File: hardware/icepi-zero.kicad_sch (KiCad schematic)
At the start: 7 parts, among them J1 Micro_SD_Card_Det2, J2 Conn_02x20_Counter_Clockwise, U1 ECP5U_12_CABGA256

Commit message: Routed most of sdram
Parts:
- removed unit 5 of U1
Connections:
- net A10: now reaches U1.A10 (PT42B/-)
- net BA0: now reaches U1.A11 (PT53A/+)
- net ~{RAS}: now reaches U1.A12 (PT53B/-)
- net ~{WE}: now reaches U1.A13 (PT65A/+)
- net D7: now reaches U1.A14 (PT65B/-)
- net D5: now reaches U1.A15 (PT67B/-)
- net A1: now reaches U1.A9 (PT42A/+)
- net A0: now reaches U1.B10 (PT44A/+)
- net BA1: now reaches U1.B11 (PT49A/+)
- net ~{CS}: now reaches U1.B12 (PT56A/+)
- net ~{CAS}: now reaches U1.B13 (PT60A/+)
- net DQM0: now reaches U1.B14 (PT67A/+)
- net A4: now reaches U1.B8 (PT35B/-/PCLKC1_0)
- net A2: now reaches U1.B9 (PT38A/+/GR_PCLK1_0)
- net GLOBAL_CLK: now reaches U1.M2 (PL26D/-/PCLKC6_0/LDQ32)
- net D6: now reaches U1.B15 (PR2B/-/S0_IN/HS/RDQ8)
- net D0: now reaches U1.B16 (PR2A/+/HS/RDQ8)
- net D1: now reaches U1.C14 (PR2C/+/RDQ8)
- net D3: now reaches U1.C15 (PR5B/-/HS/RDQ8)
- net D2: now reaches U1.C16 (PR5A/+/HS/RDQ8)
- net D4: now reaches U1.D16 (PR8A/+/HS/RDQS8)
- net D8: now reaches U1.A2 (PT4A/+)
- net CLK: now reaches U1.A3 (PT6A/+)
- net A12: now reaches U1.A4 (PT6B/-)
- net A9: now reaches U1.A5 (PT18A/+)
- net A7: now reaches U1.A6 (PT18B/-)
- net A5: now reaches U1.A7 (PT29A/+/PCLKT0_0)
- net A3: now reaches U1.A8 (PT29B/-/PCLKC0_0)
- net DQM1: now reaches U1.B3 (PT4B/-)
- net CKE: now reaches U1.B4 (PT11B/-)
- net A11: now reaches U1.B5 (PT15B/-)
- net A8: now reaches U1.B6 (PT22B/-)
- net A6: now reaches U1.B7 (PT27B/-/PCLKC0_1)
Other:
- note added: "Maybe add a wifi module"

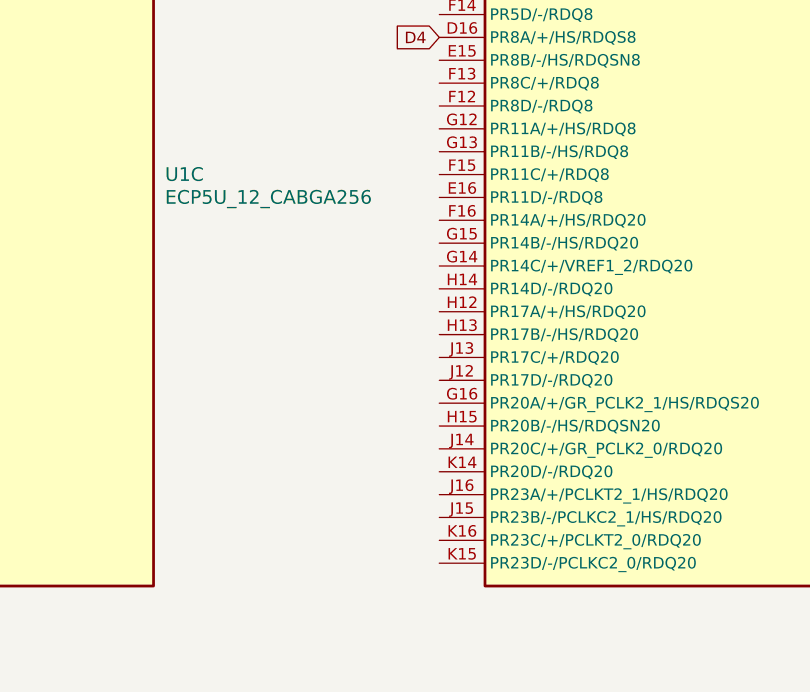
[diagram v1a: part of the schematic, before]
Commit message: Routed power
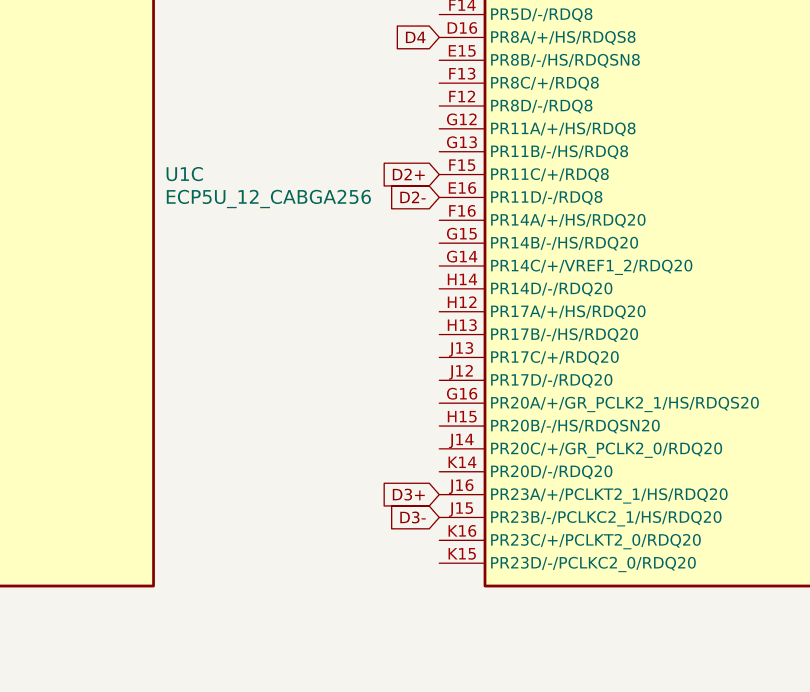
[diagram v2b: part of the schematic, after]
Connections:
- net D2-: now reaches U1.E16 (PR11D/-/RDQ8)
- net D2+: now reaches U1.F15 (PR11C/+/RDQ8)
- net D3-: now reaches U1.J15 (PR23B/-/PCLKC2_1/HS/RDQ20)
- net D3+: now reaches U1.J16 (PR23A/+/PCLKT2_1/HS/RDQ20)
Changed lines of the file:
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@@
+		)
+	)
+	(global_label "D2+"
+		(shape input)
+		(at 416.56 52.07 180)
+		(fields_autoplaced yes)
+		(effects
+			(font
+				(size 1.27 1.27)
+			)
+			(justify right)
+		)
+		(property "Intersheetrefs" "${INTERSHEET_REFS}"
+			(at 409.5229 52.07 0)
+			(effects
+				(font
+					(size 1.27 1.27)
+				)
+				(justify right)
+				(hide yes)
+			)
 		)
 	)
@@
 		)
 	)
+	(global_label "D3-"
+		(shape input)
+		(at 416.56 90.17 180)
+		(fields_autoplaced yes)
+		(effects
+			(font
+				(size 1.27 1.27)
+			)
+			(justify right)
+		)
+		(property "Intersheetrefs" "${INTERSHEET_REFS}"
+			(at 409.5229 90.17 0)
+			(effects
+				(font
+					(size 1.27 1.27)
+				)
+				(justify right)
+				(hide yes)
+			)
+		)
+	)
 	(global_label "A6"
 		(shape input)
@@
 			(effects
 				(font
+					(size 1.27 1.27)
+				)
+				(justify right)
+				(hide yes)
+			)
+		)
+	)
+	(global_label "D2-"
+		(shape input)
+		(at 416.56 54.61 180)
+		(fields_autoplaced yes)
+		(effects
+			(font
+				(size 1.27 1.27)
+			)
+			(justify right)
+		)
+		(property "Intersheetrefs" "${INTERSHEET_REFS}"
+			(at 409.5229 54.61 0)
+			(effects
+				(font
+					(size 1.27 1.27)
+				)
+				(justify right)
+				(hide yes)
+			)
+		)
+	)
+	(global_label "D3+"
+		(shape input)
+		(at 416.56 87.63 180)
+		(fields_autoplaced yes)
+		(effects
+			(font
+				(size 1.27 1.27)
+			)
+			(justify right)
+		)
+		(property "Intersheetrefs" "${INTERSHEET_REFS}"
+			(at 409.5229 87.63 0)
+			(effects
+				(font

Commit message: Added the decoupling capacitors
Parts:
- added C35, C41, C42: 10uF, Capacitor_SMD:C_0603_1608Metric, symbol Device:C_Small
- added C36, C37, C39, C40: 100nF, Capacitor_SMD:C_0402_1005Metric, symbol Device:C_Small
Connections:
- net +3V3: now also J1.4 (VDD), U1.F10 (VCCIO1[2]), U1.F11 (VCCIO1[2]), U1.F6 (VCCIO0[2]), U1.F7 (VCCIO0[2]), U1.H11 (VCCIO2[2]), U1.J11 (VCCIO2[2]), U1.J6 (VCCIO6[2]), U1.J7 (VCCIO6[2]), C35.1, C36.1, C37.1, C39.1, C40.1, C41.1, C42.1
- net CLK: now also J1.5 (CLK)
- net GND: now also J1.11 (SHIELD), J1.6 (VSS), J1.9 (DET_B), C35.2, C36.2, C37.2, C39.2, C40.2, C41.2, C42.2
- net GPIO_10: now reaches J2.10 (Pin_10)
- net GPIO_10: now also U1.N1 (PL32A/+/HS/LDQS32)
- net GPIO_11: now reaches J2.11 (Pin_11)
- net GPIO_11: now also U1.R4 (PL41C/+/LDQ44)
- net GPIO_12: now reaches J2.12 (Pin_12)
- net GPIO_12: now also U1.N4 (PL38A/+/HS/LDQ44)
- net GPIO_13: now reaches J2.13 (Pin_13)
- net GPIO_13: now also U1.P4 (PL41A/+/HS/LDQ44)
- net GPIO_15: now reaches J2.15 (Pin_15)
- net GPIO_15: now also U1.P2 (PL32B/-/HS/LDQSN32)
- net GPIO_16: now reaches J2.16 (Pin_16)
- net GPIO_16: now also U1.M1 (PL26C/+/PCLKT6_0/LDQ32)
- net GPIO_18: now reaches J2.18 (Pin_18)
- net GPIO_18: now also U1.L1 (PL26A/+/PCLKT6_1/HS/LDQ32)
- net GPIO_19: now reaches J2.19 (Pin_19)
- net GPIO_21: now reaches J2.21 (Pin_21)
- net GPIO_22: now reaches J2.22 (Pin_22)
- net GPIO_23: now reaches J2.23 (Pin_23)
- net GPIO_24: now reaches J2.24 (Pin_24)
- net GPIO_26: now reaches J2.26 (Pin_26)
- net GPIO_27: now reaches J2.27 (Pin_27)
- net GPIO_28: now reaches J2.28 (Pin_28)
- net GPIO_29: now reaches J2.29 (Pin_29)
- net GPIO_3: now reaches J2.3 (Pin_3)
- net GPIO_3: now also U1.T2 (PL38D/-/LDQ44)
- net GPIO_31: now reaches J2.31 (Pin_31)
- net GPIO_32: now reaches J2.32 (Pin_32)
- net GPIO_33: now reaches J2.33 (Pin_33)
- net GPIO_35: now reaches J2.35 (Pin_35)
- net GPIO_36: now reaches J2.36 (Pin_36)
- net GPIO_37: now reaches J2.37 (Pin_37)
- net GPIO_37: now also U1.C4 (PT11A/+)
- net GPIO_38: now reaches J2.38 (Pin_38)
- net GPIO_40: now reaches J2.40 (Pin_40)
- net GPIO_5: now reaches J2.5 (Pin_5)
- net GPIO_5: now also U1.R2 (PL38C/+/LDQ44)
- net GPIO_7: now reaches J2.7 (Pin_7)
- net GPIO_7: now also U1.R1 (PL35B/-/VREF1_6/HS/LDQ32)
- net GPIO_8: now reaches J2.8 (Pin_8)
- net GPIO_8: now also U1.P1 (PL35A/+/HS/LDQ32)
- net FPDI_SCL: now reaches U1.T3 (PL41D/-/LDQ44)
- net FPDI_SDA: now reaches U1.T4 (PL44B/-/HS/LDQSN44)
- net DAT2: now reaches J1.1 (DAT2)
- net DET: now reaches J1.10 (DET_A)
- net DAT3: now reaches J1.2 (DAT3/CD)
- net CMD: now reaches J1.3 (CMD)
- net DAT0: now reaches J1.7 (DAT0)
- net DAT1: now reaches J1.8 (DAT1)
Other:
- moved on the sheet: J1

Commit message: V1.0 Final Revision and Readme documentation
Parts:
- removed C37, C39, C40: 100nF, Capacitor_SMD:C_0402_1005Metric, symbol Device:C_Small
- removed C41, C42: 10uF, Capacitor_SMD:C_0603_1608Metric, symbol Device:C_Small
- removed J1: Micro_SD_Card_Det2, icepi-lib:microSD_HC_SOFNG_TF-008, symbol Connector:Micro_SD_Card_Det2
- removed U1: ECP5U_12_CABGA256, Package_BGA:BGA-256_14.0x14.0mm_Layout16x16_P0.8mm_Ball0.45mm_Pad0.32mm_NSMD, symbol josh:ECP5U_12_CABGA256
- added D1, D2, D3, D4: WHITE, LED_SMD:LED_0603_1608Metric, symbol Device:LED
- added R1, R2, R3, R4: 470, Resistor_SMD:R_0402_1005Metric, symbol Device:R
- added TP1, TP2, TP3, TP4, TP5, TP6: TestPoint, TestPoint:TestPoint_Pad_D2.0mm, symbol Connector:TestPoint
- added U3: ECP5U_12_CABGA256, Package_BGA:BGA-256_14.0x14.0mm_Layout16x16_P0.8mm_Ball0.45mm_Pad0.32mm_NSMD, symbol josh:ECP5U_12_CABGA256
- renumbered C35 to C47, C36 to C48, J2 to J1
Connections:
- net +3V3: now also TP2.1, U3.J6 (VCCIO6[2]), U3.J7 (VCCIO6[2])
- net +5V: now also TP1.1
- net FPDI_SCL: now also U3.T3 (PL41D/-/LDQ44)
- net FPDI_SDA: now also U3.T4 (PL44B/-/HS/LDQSN44)
- net GLOBAL_CLK: now also U3.M2 (PL26D/-/PCLKC6_0/LDQ32)
- net GND: now also D1.1 (K), D2.1 (K), D3.1 (K), D4.1 (K), TP4.1, TP5.1
- net GPIO_10: now also U3.N1 (PL32A/+/HS/LDQS32)
- net GPIO_11: now also U3.R3 (PL41B/-/HS/LDQ44)
- net GPIO_12: now also U3.N4 (PL38A/+/HS/LDQ44)
- net GPIO_13: now also U3.P3 (PL38B/-/HS/LDQ44)
- net GPIO_15: now also U3.P2 (PL32B/-/HS/LDQSN32)
- net GPIO_16: now also U3.M1 (PL26C/+/PCLKT6_0/LDQ32)
- net GPIO_18: now also U3.L1 (PL26A/+/PCLKT6_1/HS/LDQ32)
- net GPIO_3: now also U3.T2 (PL38D/-/LDQ44)
- net GPIO_5: now also U3.R2 (PL38C/+/LDQ44)
- net GPIO_7: now also U3.R1 (PL35B/-/VREF1_6/HS/LDQ32)
- net GPIO_8: now also U3.P1 (PL35A/+/HS/LDQ32)
- new net: D1.2 (A), R1.2
- new net: D2.2 (A), R2.2
- new net: D4.2 (A), R4.2
- new net: D3.2 (A), R3.2
- new net +1V1: TP3.1
- new net +2V5: TP6.1
- new net FPDI_CEC: U3.R5 (PL44A/+/HS/LDQS44)
- new net FPDI_UTIL: U3.P5 (PL47D/-/LLC_GPLL0C_IN/LDQ44)
- new net LED1: R1.1
- new net LED2: R2.1
- new net LED3: R3.1
- new net LED4: R4.1
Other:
- added sheet ECP5 (ecp5.kicad_sch)
- note removed: "TODO: Check out how to add WiFI"
- moved on the sheet: C47, C48, H1, H2, H3, H4

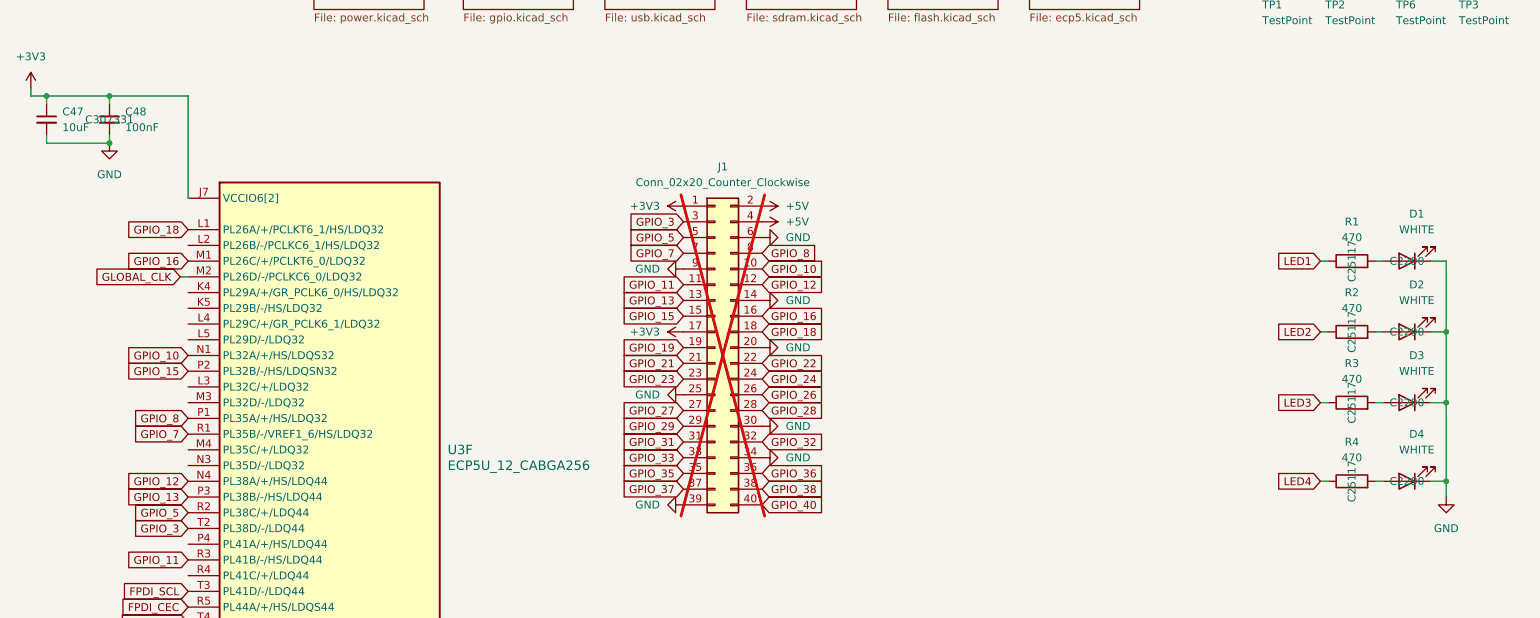
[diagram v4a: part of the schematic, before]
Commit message: Fix level shifter EN voltage error
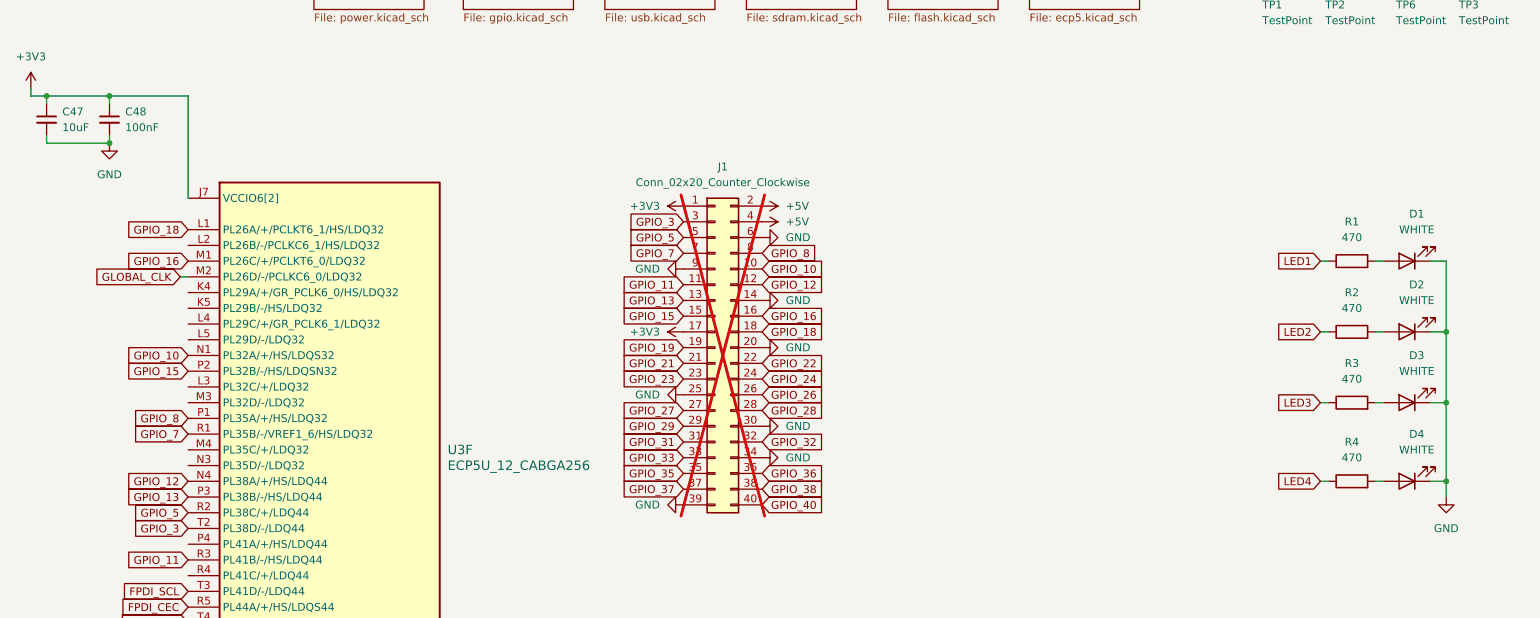
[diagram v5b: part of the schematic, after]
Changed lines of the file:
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@@
 					(size 1.27 1.27)
 				)
+				(hide yes)
 			)
 		)
@@
 					(size 1.27 1.27)
 				)
+				(hide yes)
 			)
 		)
@@
 					(size 1.27 1.27)
 				)
+				(hide yes)
 			)
 		)
@@
 					(size 1.27 1.27)
 				)
+				(hide yes)
 			)
 		)
@@
 					(size 1.27 1.27)
 				)
+				(hide yes)
 			)
 		)
@@
 					(size 1.27 1.27)
 				)
+				(hide yes)
 			)
 		)
@@
 					(size 1.27 1.27)
 				)
+				(hide yes)
 			)
 		)
@@
 					(size 1.27 1.27)
 				)
+				(hide yes)
 			)
 		)
@@
 					(size 1.27 1.27)
 				)
-			)
-		)
+				(hide yes)
+			)
+		)

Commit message: Add a revision
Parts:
- TP1, TP2, TP3, TP4, TP5, TP6: now not fitted
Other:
- note removed: "Maybe add a wifi module"
- moved on the sheet: D1, D2, D3, D4, R1, R2, R3, R4

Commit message: Pre-prod fixes
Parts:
- added D6: WHITE, LED_SMD:LED_0603_1608Metric, symbol Device:LED
- added R34: 470, Resistor_SMD:R_0402_1005Metric, symbol Device:R
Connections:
- net GND: now also D6.1 (K)
- net GPIO_19: now also U3.L2 (PL26B/-/PCLKC6_1/HS/LDQ32)
- net LED2: now also R4.1; no longer R2.1
- net LED3: now also R2.1; no longer R3.1
- net LED4: now also R3.1; no longer R4.1
- new net: D6.2 (A), R34.2
- new net LED5: R34.1

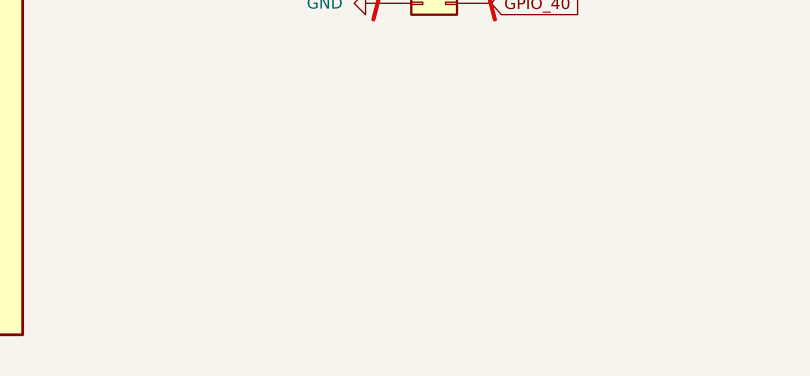
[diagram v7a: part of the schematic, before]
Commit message: Add a button
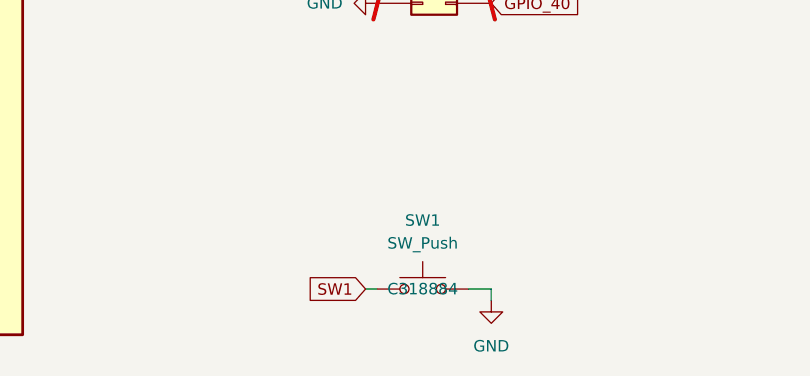
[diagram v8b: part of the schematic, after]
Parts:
- added SW1: SW_Push, Button_Switch_SMD:SW_SPST_TL3342, symbol Switch:SW_Push
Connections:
- net GND: now also SW1.2
- new net SW1: SW1.1
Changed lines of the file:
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@@
 	(wire
 		(pts
+			(xy 139.7 176.53) (xy 142.24 176.53)
+		)
+		(stroke
+			(width 0)
+			(type default)
+		)
+	)
+	(wire
+		(pts
 			(xy 203.2 113.03) (xy 204.47 113.03)
 		)
@@
 	(wire
 		(pts
+			(xy 142.24 177.8) (xy 142.24 176.53)
+		)
+		(stroke
+			(width 0)
+			(type default)
+		)
+	)
+	(wire
+		(pts
 			(xy 212.09 113.03) (xy 213.36 113.03)
 		)
@@
 	(wire
 		(pts
+			(xy 128.27 176.53) (xy 129.54 176.53)
+		)
+		(stroke
+			(width 0)
+			(type default)
+		)
+	)
+	(wire
+		(pts
 			(xy 212.09 137.16) (xy 213.36 137.16)
 		)
@@
 		)
 	)
+	(global_label "SW1"
+		(shape input)
+		(at 128.27 176.53 180)
+		(fields_autoplaced yes)
+		(effects
+			(font
+				(size 1.27 1.27)
+			)
+			(justify right)
+		)
+		(property "Intersheetrefs" "${INTERSHEET_REFS}"
+			(at 121.4144 176.53 0)
+			(effects
+				(font
+					(size 1.27 1.27)
+				)
+				(justify right)
+				(hide yes)
+			)
+		)
+	)
 	(global_label "LED1"
 		(shape input)
@@
 	)
 	(symbol
+		(lib_id "power:GND")
+		(at 142.24 177.8 0)
+		(unit 1)
+		(exclude_from_sim no)
+		(in_bom yes)
+		(on_board yes)
+		(dnp no)
+		(fields_autoplaced yes)
+		(property "Reference" "#PWR0100"
+			(at 142.24 184.15 0)
+			(effects
+				(font
+					(size 1.27 1.27)
+				)
+				(hide yes)
+			)
+		)
+		(property "Value" "GND"
+			(at 142.24 182.88 0)
+			(effects
+				(font
+					(size 1.27 1.27)
+				)
+			)
+		)
+		(property "Footprint" ""
+			(at 142.24 177.8 0)
+			(effects
+				(font
+					(size 1.27 1.27)
+				)
+				(hide yes)
+			)
+		)
+		(property "Datasheet" ""
+			(at 142.24 177.8 0)
+			(effects
+				(font
+					(size 1.27 1.27)
+				)
+				(hide yes)
+			)
+		)
+		(property "Description" "Power symbol creates a global label with name \"GND\" , ground"
+			(at 142.24 177.8 0)
+			(effects
+				(font
+					(size 1.27 1.27)
+				)
+				(hide yes)
+			)
+		)
+		(pin "1"
+		)
+		(instances
+			(project ""
+				(path "/f88da08e-cf42-4d03-a08f-3f602fe6658d"
+					(reference "#PWR0100")
+					(unit 1)
+				)
+			)
+		)
+	)
+	(symbol
 		(lib_id "josh:ECP5U_12_CABGA256")
 		(at 71.12 133.35 0)
@@
 					(unit 1)
 				)
+			)
+		)
+	)
+	(symbol
+		(lib_id "Switch:SW_Push")
+		(at 134.62 176.53 0)
+		(unit 1)
+		(exclude_from_sim no)
+		(in_bom yes)
+		(on_board yes)
+		(dnp no)
+		(fields_autoplaced yes)
+		(property "Reference" "SW1"
+			(at 134.62 168.91 0)
+			(effects
+				(font
+					(size 1.27 1.27)
+				)
+			)
+		)
+		(property "Value" "SW_Push"
+			(at 134.62 171.45 0)
+			(effects
+				(font
+					(size 1.27 1.27)
+				)
+			)
+		)
+		(property "Footprint" "Button_Switch_SMD:SW_SPST_TL3342"
+			(at 134.62 171.45 0)
+			(effects
+				(font
+					(size 1.27 1.27)
+				)
+				(hide yes)
+			)
+		)
+		(property "Datasheet" "~"
+			(at 134.62 171.45 0)
+			(effects
+				(font
+					(size 1.27 1.27)
+				)
+				(hide yes)
+			)
+		)
+		(property "Description" "Push button switch, generic, two pins"
+			(at 134.62 176.53 0)
+			(effects
+				(font
+					(size 1.27 1.27)
+				)
+				(hide yes)
+			)
+		)
+		(property "JLCPCB Part #" "C318884"
+			(at 134.62 176.53 0)
+			(effects
+				(font
+					(size 1.27 1.27)
+				)
+			)
+		)
+		(pin "2"
+		)
+		(pin "1"
+		)
+		(instances
+			(project ""
+				(path "/f88da08e-cf42-4d03-a08f-3f602fe6658d"
+					(reference "SW1")
+					(unit 1)
+				)
